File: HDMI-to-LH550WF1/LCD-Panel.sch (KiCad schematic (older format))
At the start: 15 parts, among them P3 LH550WF1, U3 TPS65132A0YFF, U4 TPS61161

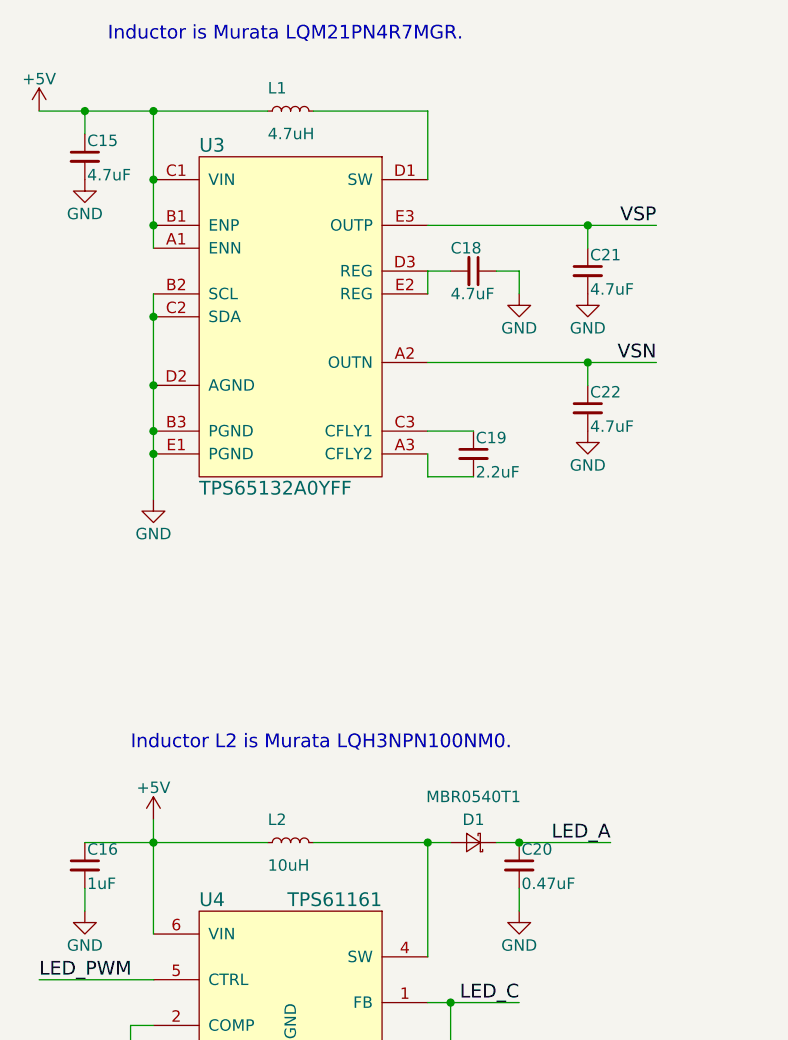
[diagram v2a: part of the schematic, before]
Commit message: Fixed issues in LCD panel sheet
- Replaced inductor values with part numbers.
- Swapped one 0603 cap for an 0402 one.
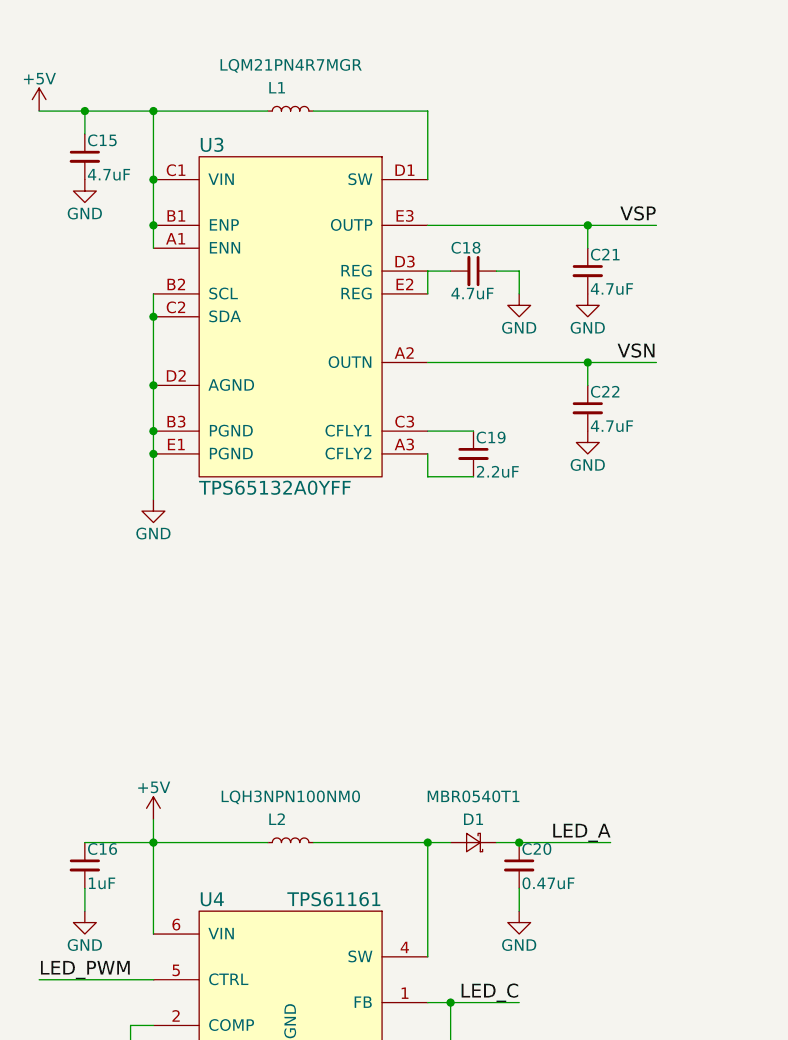
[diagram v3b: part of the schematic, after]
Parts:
- C16: footprint Capacitors_SMD:C_0603 -> Capacitors_SMD:C_0402
- L1: value 4.7uH -> LQM21PN4R7MGR
- L2: value 10uH -> LQH3NPN100NM0
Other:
- note removed: "Inductor L2 is Murata LQH3NPN100NM0."
- note removed: "Inductor is Murata LQM21PN4R7MGR."
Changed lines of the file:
@@
 F 0 "C16" H 2310 4770 50  0000 L CNN
 F 1 "1uF" H 2310 4620 50  0000 L CNN
-F 2 "Capacitors_SMD:C_0603" H 2300 4700 50  0001 C CNN
+F 2 "Capacitors_SMD:C_0402" H 2300 4700 50  0001 C CNN
 F 3 "" H 2300 4700 50  0000 C CNN
 	1    2300 4700
@@
 P 3200 4600
 F 0 "L2" V 3300 4700 50  0000 R CNN
-F 1 "10uH" V 3100 4700 50  0000 R CNN
+F 1 "LQH3NPN100NM0" V 3400 4600 50  0000 C CNN
 F 2 "Inductors:Inductor_Taiyo-Yuden_MD-3030" H 3200 4600 50  0001 C CNN
 F 3 "" H 3200 4600 50  0000 C CNN
@@
 Connection ~ 4200 4600
 Connection ~ 3900 5300
-Text Notes 2500 4200 0    60   ~ 0
-Inductor L2 is Murata LQH3NPN100NM0.
 $Comp
 L +5V #PWR037
@@
 P 3200 1400
 F 0 "L1" V 3300 1500 50  0000 R CNN
-F 1 "4.7uH" V 3100 1500 50  0000 R CNN
+F 1 "LQM21PN4R7MGR" V 3400 1400 50  0000 C CNN
 F 2 "Resistors_SMD:R_0805" H 3200 1400 50  0001 C CNN
 F 3 "" H 3200 1400 50  0000 C CNN
@@
 Connection ~ 2600 2600
 Connection ~ 2600 2300
-Text Notes 2400 1100 0    60   ~ 0
-Inductor is Murata LQM21PN4R7MGR.
 $EndSCHEMATC
